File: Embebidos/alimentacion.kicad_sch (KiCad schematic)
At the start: 20 parts, among them J1 Conn_01x02_Male, J2 Conn_01x02_Male, J4 Conn_01x02_Male, U1 MIC29302WT, U2 SPX3819M5-L-3-3, U4 MIC5219-3.3YM5

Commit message: Alimentacion
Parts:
- C1: value 100u -> (none)
- C10, C5, C7: value 10u -> (none)
- C11: value 0.1u -> (none)
- C2: value 1u -> (none); footprint Capacitor_SMD:C_0603_1608Metric_Pad1.08x0.95mm_HandSolder -> (none)
- C3: value 330u -> (none)
- C4: value 100n -> (none)
- C6: value 1u -> (none)
- J1, J2, J4: value Conn_01x02_Male -> (none)
- R1: value 100k -> (none)
- R2: value 43k -> (none)
- R3: value 470 -> (none)
- R4, R5: value R -> (none)
- U1: value MIC29302WT -> (none); footprint Package_TO_SOT_THT:TO-220-5_P3.4x3.7mm_StaggerEven_Lead3.8mm_Vertical -> (none)
- U2: value SPX3819M5-L-3-3 -> (none); footprint Package_TO_SOT_SMD:SOT-23-5 -> (none)
- U4: value MIC5219-3.3YM5 -> (none); footprint Package_TO_SOT_SMD:SOT-23-5 -> (none)
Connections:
- net Esp32: no longer U2.3 (EN), U4.3 (EN)
- net +3.3V renamed 3.3
- new net CtrlOnOff: U2.3 (EN), U4.3 (EN)

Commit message: Alimentacion
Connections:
- net 3.3 renamed +3.3V
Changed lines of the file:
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@@
   (junction (at 153.035 142.24) (diameter 0) (color 0 0 0 0)
   )
+  (junction (at 45.72 81.28) (diameter 0) (color 0 0 0 0)
+  )
   (junction (at 195.58 81.28) (diameter 0) (color 0 0 0 0)
   )
@@
   )
   (junction (at 134.62 163.195) (diameter 0) (color 0 0 0 0)
-  )
-  (junction (at 45.72 80.01) (diameter 0) (color 0 0 0 0)
   )
   (junction (at 139.7 81.28) (diameter 0) (color 0 0 0 0)
@@
     (stroke (width 0) (type default) (color 0 0 0 0))
   )
-  (wire (pts (xy 35.56 69.85) (xy 38.1 69.85))
-    (stroke (width 0) (type default) (color 0 0 0 0))
-  )
   (wire (pts (xy 191.77 142.24) (xy 191.77 146.685))
     (stroke (width 0) (type default) (color 0 0 0 0))
@@
     (stroke (width 0) (type default) (color 0 0 0 0))
   )
-  (wire (pts (xy 151.13 87.63) (xy 152.4 87.63))
-    (stroke (width 0) (type default) (color 0 0 0 0))
-  )
   (wire (pts (xy 134.62 163.195) (xy 138.43 163.195))
     (stroke (width 0) (type default) (color 0 0 0 0))
@@
     (stroke (width 0) (type default) (color 0 0 0 0))
   )
-  (wire (pts (xy 45.72 76.2) (xy 45.72 80.01))
-    (stroke (width 0) (type default) (color 0 0 0 0))
-  )
   (wire (pts (xy 182.245 153.67) (xy 182.245 163.195))
     (stroke (width 0) (type default) (color 0 0 0 0))
@@
     (stroke (width 0) (type default) (color 0 0 0 0))
   )
-  (wire (pts (xy 33.02 80.01) (xy 45.72 80.01))
+  (wire (pts (xy 33.02 81.28) (xy 45.72 81.28))
     (stroke (width 0) (type default) (color 0 0 0 0))
   )
@@
     (stroke (width 0) (type default) (color 0 0 0 0))
   )
+  (wire (pts (xy 45.72 76.2) (xy 45.72 81.28))
+    (stroke (width 0) (type default) (color 0 0 0 0))
+  )
   (wire (pts (xy 67.31 66.04) (xy 67.31 67.31))
     (stroke (width 0) (type default) (color 0 0 0 0))
@@
     (stroke (width 0) (type default) (color 0 0 0 0))
   )
-  (wire (pts (xy 33.02 68.58) (xy 33.02 80.01))
+  (wire (pts (xy 33.02 68.58) (xy 33.02 81.28))
     (stroke (width 0) (type default) (color 0 0 0 0))
   )
@@
     (stroke (width 0) (type default) (color 0 0 0 0))
   )
+  (wire (pts (xy 45.72 85.09) (xy 45.72 81.28))
+    (stroke (width 0) (type default) (color 0 0 0 0))
+  )
   (wire (pts (xy 111.76 163.195) (xy 134.62 163.195))
     (stroke (width 0) (type default) (color 0 0 0 0))
@@
     (stroke (width 0) (type default) (color 0 0 0 0))
   )
-  (global_label "3.3" (shape output) (at 195.58 77.47 0) (fields_autoplaced)
-    (effects (font (size 1.27 1.27)) (justify left))
-    (property "Intersheet References" "${INTERSHEET_REFS}" (id 0) (at 201.0169 77.3906 0)
-      (effects (font (size 1.27 1.27)) (justify left) hide)
-    )
-  )
-  (global_label "CtrlOnOff" (shape input) (at 35.56 69.85 270) (fields_autoplaced)
+  (global_label "CtrlOnOff" (shape input) (at 38.1 69.85 270) (fields_autoplaced)
     (effects (font (size 1.27 1.27)) (justify right))
-    (property "Intersheet References" "${INTERSHEET_REFS}" (id 0) (at 35.4806 80.9717 90)
+    (property "Intersheet References" "${INTERSHEET_REFS}" (id 0) (at 38.0206 80.9717 90)
       (effects (font (size 1.27 1.27)) (justify right) hide)
     )
@@
     )
   )
-  (global_label "CtrlOnOff" (shape input) (at 152.4 87.63 270) (fields_autoplaced)
+  (global_label "CtrlOnOff" (shape input) (at 151.13 87.63 270) (fields_autoplaced)
     (effects (font (size 1.27 1.27)) (justify right))
-    (property "Intersheet References" "${INTERSHEET_REFS}" (id 0) (at 152.3206 98.7517 90)
+    (property "Intersheet References" "${INTERSHEET_REFS}" (id 0) (at 151.0506 98.7517 90)
       (effects (font (size 1.27 1.27)) (justify right) hide)
     )
@@
     (property "Intersheet References" "${INTERSHEET_REFS}" (id 0) (at 124.3806 158.6533 90)
       (effects (font (size 1.27 1.27)) (justify right) hide)
-    )
-  )
-  (global_label "3.3" (shape output) (at 77.47 64.77 90) (fields_autoplaced)
-    (effects (font (size 1.27 1.27)) (justify left))
-    (property "Intersheet References" "${INTERSHEET_REFS}" (id 0) (at 77.3906 59.3331 90)
-      (effects (font (size 1.27 1.27)) (justify left) hide)
     )
   )
@@
     (pin "1")
   )
+  (symbol (lib_id "power:+3.3V") (at 77.47 64.77 0) (unit 1)
+    (in_bom yes) (on_board yes)
+    (property "Reference" "#PWR06" (id 0) (at 77.47 68.58 0)
+      (effects (font (size 1.27 1.27)) hide)
+    )
+    (property "Value" "" (id 1) (at 77.851 60.3758 0))
+    (property "Footprint" "" (id 2) (at 77.47 64.77 0)
+      (effects (font (size 1.27 1.27)) hide)
+    )
+    (property "Datasheet" "" (id 3) (at 77.47 64.77 0)
+      (effects (font (size 1.27 1.27)) hide)
+    )
+    (pin "1")
+  )
   (symbol (lib_id "Device:R") (at 67.31 82.55 0) (unit 1)
     (in_bom yes) (on_board yes) (fields_autoplaced)
@@
     (pin "2")
   )
-  (symbol (lib_id "power:GND") (at 45.72 80.01 0) (unit 1)
-    (in_bom yes) (on_board yes) (fields_autoplaced)
-    (property "Reference" "#PWR03" (id 0) (at 45.72 86.36 0)
-      (effects (font (size 1.27 1.27)) hide)
-    )
-    (property "Value" "" (id 1) (at 45.72 85.09 0))
-    (property "Footprint" "" (id 2) (at 45.72 80.01 0)
-      (effects (font (size 1.27 1.27)) hide)
-    )
-    (property "Datasheet" "" (id 3) (at 45.72 80.01 0)
+  (symbol (lib_id "power:GND") (at 45.72 85.09 0) (unit 1)
+    (in_bom yes) (on_board yes) (fields_autoplaced)
+    (property "Reference" "#PWR03" (id 0) (at 45.72 91.44 0)
+      (effects (font (size 1.27 1.27)) hide)
+    )
+    (property "Value" "" (id 1) (at 45.72 90.17 0))
+    (property "Footprint" "" (id 2) (at 45.72 85.09 0)
+      (effects (font (size 1.27 1.27)) hide)
+    )
+    (property "Datasheet" "" (id 3) (at 45.72 85.09 0)
       (effects (font (size 1.27 1.27)) hide)
     )
@@
     (pin "2")
   )
+  (symbol (lib_id "power:+3.3V") (at 195.58 77.47 0) (unit 1)
+    (in_bom yes) (on_board yes)
+    (property "Reference" "#PWR011" (id 0) (at 195.58 81.28 0)
+      (effects (font (size 1.27 1.27)) hide)
+    )
+    (property "Value" "" (id 1) (at 195.961 73.0758 0))
+    (property "Footprint" "" (id 2) (at 195.58 77.47 0)
+      (effects (font (size 1.27 1.27)) hide)
+    )
+    (property "Datasheet" "" (id 3) (at 195.58 77.47 0)
+      (effects (font (size 1.27 1.27)) hide)
+    )
+    (pin "1")
+  )
   (symbol (lib_id "power:+5V") (at 91.44 140.97 0) (unit 1)

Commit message: Corrección de anotaciones
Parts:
- C10: renamed from C5; value (none) -> 10u
- C11: renamed from C6; value (none) -> 1u
- C12: renamed from C1; value (none) -> 100u
- C13: renamed from C2; value (none) -> 1u; footprint (none) -> Capacitor_SMD:C_0603_1608Metric_Pad1.08x0.95mm_HandSolder
- C14: renamed from C7; value (none) -> 10u
- C15: renamed from C3; value (none) -> 330u
- C16: renamed from C4; value (none) -> 100n
- C17: renamed from C10; value (none) -> 10u
- C18: renamed from C11; value (none) -> 0.1u
- J2: renamed from J1; value (none) -> Conn_01x02_Male
- J3: renamed from J2; value (none) -> Conn_01x02_Male
- J4: value (none) -> Conn_01x02_Male
- R18: renamed from R4; value (none) -> R
- R19: renamed from R5; value (none) -> R
- R20: renamed from R1; value (none) -> 100k
- R21: renamed from R2; value (none) -> 43k
- R22: renamed from R3; value (none) -> 470
- U3: renamed from U2; value (none) -> SPX3819M5-L-3-3; footprint (none) -> Package_TO_SOT_SMD:SOT-23-5
- U4: renamed from U1; value (none) -> MIC29302WT; footprint (none) -> Package_TO_SOT_THT:TO-220-5_P3.4x3.7mm_StaggerEven_Lead3.8mm_Vertical
- U5: renamed from U4; value (none) -> MIC5219-3.3YM5; footprint (none) -> Package_TO_SOT_SMD:SOT-23-5
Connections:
- no-connect marks 1 -> 0

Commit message: error_elc
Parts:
- removed J2, J4: Conn_01x02_Male, symbol Connector:Conn_01x02_Male
- renumbered C12 to C1, C17 to C10, C18 to C11, C13 to C2, C15 to C3, C16 to C4, C10 to C5, C11 to C6, C14 to C7, J3 to J2, R20 to R1, R21 to R2, R22 to R3, R18 to R4, R19 to R5, U4 to U1, U3 to U2, U5 to U4
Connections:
- net +3.3V: no longer C10.1, C11.1, U4.5 (OUT)
- net +5V: now also C7.1, U2.1 (IN), U4.1 (IN)
- new net 3.3Vop2: C10.1, C11.1, U4.5 (OUT)
- no-connect marks 0 -> 1

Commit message: anotaciones_fix
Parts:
- renumbered C5 to C10, C6 to C11, C1 to C12, C2 to C13, C7 to C14, C3 to C15, C4 to C16, C10 to C17, C11 to C18, R4 to R19, R5 to R20, R1 to R21, R2 to R22, R3 to R23, U2 to U3, U1 to U4, U4 to U5
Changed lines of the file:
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@@
   (symbol (lib_id "power:GND") (at 138.43 168.275 0) (unit 1)
     (in_bom yes) (on_board yes) (fields_autoplaced)
-    (property "Reference" "#PWR02" (id 0) (at 138.43 174.625 0)
+    (property "Reference" "#PWR031" (id 0) (at 138.43 174.625 0)
       (effects (font (size 1.27 1.27)) hide)
     )
@@
   (symbol (lib_id "Device:C") (at 139.7 87.63 0) (unit 1)
     (in_bom yes) (on_board yes) (fields_autoplaced)
-    (property "Reference" "C7" (id 0) (at 143.51 86.3599 0)
+    (property "Reference" "C14" (id 0) (at 143.51 86.3599 0)
       (effects (font (size 1.27 1.27)) (justify left))
     )
@@
   (symbol (lib_id "power:GND") (at 67.31 90.17 0) (unit 1)
     (in_bom yes) (on_board yes) (fields_autoplaced)
-    (property "Reference" "#PWR05" (id 0) (at 67.31 96.52 0)
+    (property "Reference" "#PWR026" (id 0) (at 67.31 96.52 0)
       (effects (font (size 1.27 1.27)) hide)
     )
@@
   (symbol (lib_id "Regulator_Linear:MIC29302WT") (at 134.62 144.78 0) (unit 1)
     (in_bom yes) (on_board yes)
-    (property "Reference" "U1" (id 0) (at 134.62 134.62 0))
+    (property "Reference" "U4" (id 0) (at 134.62 134.62 0))
     (property "Value" "MIC29302WT" (id 1) (at 134.62 137.16 0))
     (property "Footprint" "Package_TO_SOT_THT:TO-220-5_P3.4x3.7mm_StaggerEven_Lead3.8mm_Vertical" (id 2) (at 96.52 126.365 90)
@@
   (symbol (lib_id "power:GND") (at 139.7 96.52 0) (unit 1)
     (in_bom yes) (on_board yes) (fields_autoplaced)
-    (property "Reference" "#PWR08" (id 0) (at 139.7 102.87 0)
+    (property "Reference" "#PWR032" (id 0) (at 139.7 102.87 0)
       (effects (font (size 1.27 1.27)) hide)
     )
@@
   (symbol (lib_id "power:GND") (at 57.15 80.01 0) (unit 1)
     (in_bom yes) (on_board yes) (fields_autoplaced)
-    (property "Reference" "#PWR04" (id 0) (at 57.15 86.36 0)
+    (property "Reference" "#PWR025" (id 0) (at 57.15 86.36 0)
       (effects (font (size 1.27 1.27)) hide)
     )
@@
   (symbol (lib_id "Device:C") (at 182.245 149.86 0) (unit 1)
     (in_bom yes) (on_board yes)
-    (property "Reference" "C4" (id 0) (at 186.055 148.5899 0)
+    (property "Reference" "C16" (id 0) (at 186.055 148.5899 0)
       (effects (font (size 1.27 1.27)) (justify left))
     )
@@
   (symbol (lib_id "power:GND") (at 162.56 99.06 0) (unit 1)
     (in_bom yes) (on_board yes) (fields_autoplaced)
-    (property "Reference" "#PWR010" (id 0) (at 162.56 105.41 0)
+    (property "Reference" "#PWR033" (id 0) (at 162.56 105.41 0)
       (effects (font (size 1.27 1.27)) hide)
     )
@@
   (symbol (lib_id "Device:C") (at 195.58 93.98 0) (unit 1)
     (in_bom yes) (on_board yes) (fields_autoplaced)
-    (property "Reference" "C11" (id 0) (at 199.39 92.7099 0)
+    (property "Reference" "C18" (id 0) (at 199.39 92.7099 0)
       (effects (font (size 1.27 1.27)) (justify left))
     )
@@
   (symbol (lib_id "Device:C") (at 111.76 148.59 0) (unit 1)
     (in_bom yes) (on_board yes) (fields_autoplaced)
-    (property "Reference" "C2" (id 0) (at 115.57 147.3199 0)
+    (property "Reference" "C13" (id 0) (at 115.57 147.3199 0)
       (effects (font (size 1.27 1.27)) (justify left))
     )
@@
   (symbol (lib_id "Device:R") (at 153.035 148.59 0) (unit 1)
     (in_bom yes) (on_board yes) (fields_autoplaced)
-    (property "Reference" "R1" (id 0) (at 155.575 147.3199 0)
+    (property "Reference" "R21" (id 0) (at 155.575 147.3199 0)
       (effects (font (size 1.27 1.27)) (justify left))
     )
@@
   (symbol (lib_id "Device:R") (at 191.77 150.495 0) (unit 1)
     (in_bom yes) (on_board yes)
-    (property "Reference" "R3" (id 0) (at 194.31 149.2249 0)
+    (property "Reference" "R23" (id 0) (at 194.31 149.2249 0)
       (effects (font (size 1.27 1.27)) (justify left))
     )
@@
   (symbol (lib_id "Device:R") (at 67.31 71.12 0) (unit 1)
     (in_bom yes) (on_board yes) (fields_autoplaced)
-    (property "Reference" "R4" (id 0) (at 69.85 69.8499 0)
+    (property "Reference" "R19" (id 0) (at 69.85 69.8499 0)
       (effects (font (size 1.27 1.27)) (justify left))
     )
@@
   (symbol (lib_id "power:GND") (at 77.47 78.74 0) (unit 1)
     (in_bom yes) (on_board yes) (fields_autoplaced)
-    (property "Reference" "#PWR07" (id 0) (at 77.47 85.09 0)
+    (property "Reference" "#PWR028" (id 0) (at 77.47 85.09 0)
       (effects (font (size 1.27 1.27)) hide)
     )
@@
   (symbol (lib_id "power:+3.3V") (at 77.47 64.77 0) (unit 1)
     (in_bom yes) (on_board yes)
-    (property "Reference" "#PWR06" (id 0) (at 77.47 68.58 0)
+    (property "Reference" "#PWR027" (id 0) (at 77.47 68.58 0)
       (effects (font (size 1.27 1.27)) hide)
     )
@@
   (symbol (lib_id "Device:R") (at 67.31 82.55 0) (unit 1)
     (in_bom yes) (on_board yes) (fields_autoplaced)
-    (property "Reference" "R5" (id 0) (at 69.85 81.2799 0)
+    (property "Reference" "R20" (id 0) (at 69.85 81.2799 0)
       (effects (font (size 1.27 1.27)) (justify left))
     )
@@
   (symbol (lib_id "power:GND") (at 45.72 85.09 0) (unit 1)
     (in_bom yes) (on_board yes) (fields_autoplaced)
-    (property "Reference" "#PWR03" (id 0) (at 45.72 91.44 0)
+    (property "Reference" "#PWR024" (id 0) (at 45.72 91.44 0)
       (effects (font (size 1.27 1.27)) hide)
     )
@@
   (symbol (lib_id "Device:R") (at 153.035 158.115 0) (unit 1)
     (in_bom yes) (on_board yes) (fields_autoplaced)
-    (property "Reference" "R2" (id 0) (at 155.575 156.8449 0)
+    (property "Reference" "R22" (id 0) (at 155.575 156.8449 0)
       (effects (font (size 1.27 1.27)) (justify left))
     )
@@
   (symbol (lib_id "Device:C_Polarized_Small_US") (at 171.45 149.86 0) (unit 1)
     (in_bom yes) (on_board yes)
-    (property "Reference" "C3" (id 0) (at 174.625 148.1581 0)
+    (property "Reference" "C15" (id 0) (at 174.625 148.1581 0)
       (effects (font (size 1.27 1.27)) (justify left))
     )
@@
   (symbol (lib_id "Regulator_Linear:SPX3819M5-L-3-3") (at 45.72 68.58 0) (unit 1)
     (in_bom yes) (on_board yes) (fields_autoplaced)
-    (property "Reference" "U2" (id 0) (at 45.72 58.42 0))
+    (property "Reference" "U3" (id 0) (at 45.72 58.42 0))
     (property "Value" "SPX3819M5-L-3-3" (id 1) (at 45.72 60.96 0))
     (property "Footprint" "Package_TO_SOT_SMD:SOT-23-5" (id 2) (at 45.72 60.325 0)
@@
   (symbol (lib_id "power:+5V") (at 135.89 73.66 0) (unit 1)
     (in_bom yes) (on_board yes) (fields_autoplaced)
-    (property "Reference" "#PWR0101" (id 0) (at 135.89 77.47 0)
-      (effects (font (size 1.27 1.27)) hide)
-    )
-    (property "Value" "+5V" (id 1) (at 135.89 68.58 0))
+    (property "Reference" "#PWR030" (id 0) (at 135.89 77.47 0)
+      (effects (font (size 1.27 1.27)) hide)
+    )
+    (property "Value" "" (id 1) (at 135.89 68.58 0))
     (property "Footprint" "" (id 2) (at 135.89 73.66 0)
       (effects (font (size 1.27 1.27)) hide)
@@
   (symbol (lib_id "Device:C") (at 57.15 73.66 0) (unit 1)
     (in_bom yes) (on_board yes) (fields_autoplaced)
-    (property "Reference" "C5" (id 0) (at 60.96 72.3899 0)
+    (property "Reference" "C10" (id 0) (at 60.96 72.3899 0)
       (effects (font (size 1.27 1.27)) (justify left))
     )
@@
   (symbol (lib_id "Regulator_Linear:MIC5219-3.3YM5") (at 162.56 83.82 0) (unit 1)
     (in_bom yes) (on_board yes) (fields_autoplaced)
-    (property "Reference" "U4" (id 0) (at 162.56 73.66 0))
+    (property "Reference" "U5" (id 0) (at 162.56 73.66 0))
     (property "Value" "MIC5219-3.3YM5" (id 1) (at 162.56 76.2 0))
     (property "Footprint" "Package_TO_SOT_SMD:SOT-23-5" (id 2) (at 162.56 75.565 0)
@@
   (symbol (lib_id "Device:C_Polarized_Small_US") (at 100.33 148.59 0) (unit 1)
     (in_bom yes) (on_board yes)
-    (property "Reference" "C1" (id 0) (at 103.505 146.8881 0)
+    (property "Reference" "C12" (id 0) (at 103.505 146.8881 0)
       (effects (font (size 1.27 1.27)) (justify left))
     )
@@
   (symbol (lib_id "power:+5V") (at 33.02 63.5 0) (unit 1)
     (in_bom yes) (on_board yes) (fields_autoplaced)
-    (property "Reference" "#PWR0102" (id 0) (at 33.02 67.31 0)
-      (effects (font (size 1.27 1.27)) hide)
-    )
-    (property "Value" "+5V" (id 1) (at 33.02 58.42 0))
+    (property "Reference" "#PWR023" (id 0) (at 33.02 67.31 0)
+      (effects (font (size 1.27 1.27)) hide)
+    )
+    (property "Value" "" (id 1) (at 33.02 58.42 0))
     (property "Footprint" "" (id 2) (at 33.02 63.5 0)
       (effects (font (size 1.27 1.27)) hide)
@@
   (symbol (lib_id "Device:C") (at 182.88 93.98 0) (unit 1)
     (in_bom yes) (on_board yes) (fields_autoplaced)
-    (property "Reference" "C10" (id 0) (at 186.69 92.7099 0)
+    (property "Reference" "C17" (id 0) (at 186.69 92.7099 0)
       (effects (font (size 1.27 1.27)) (justify left))
     )
@@
   (symbol (lib_id "Device:C_Polarized") (at 77.47 72.39 0) (unit 1)
     (in_bom yes) (on_board yes) (fields_autoplaced)
-    (property "Reference" "C6" (id 0) (at 81.28 70.2309 0)
+    (property "Reference" "C11" (id 0) (at 81.28 70.2309 0)
       (effects (font (size 1.27 1.27)) (justify left))
     )
@@
   (symbol (lib_id "power:+5V") (at 91.44 140.97 0) (unit 1)
     (in_bom yes) (on_board yes) (fields_autoplaced)
-    (property "Reference" "#PWR01" (id 0) (at 91.44 144.78 0)
-      (effects (font (size 1.27 1.27)) hide)
-    )
+    (property "Reference" "#PWR029" (id 0) (at 91.44 144.78 0)
+      (effects (font (size 1.27 1.27)) hide)
+    )

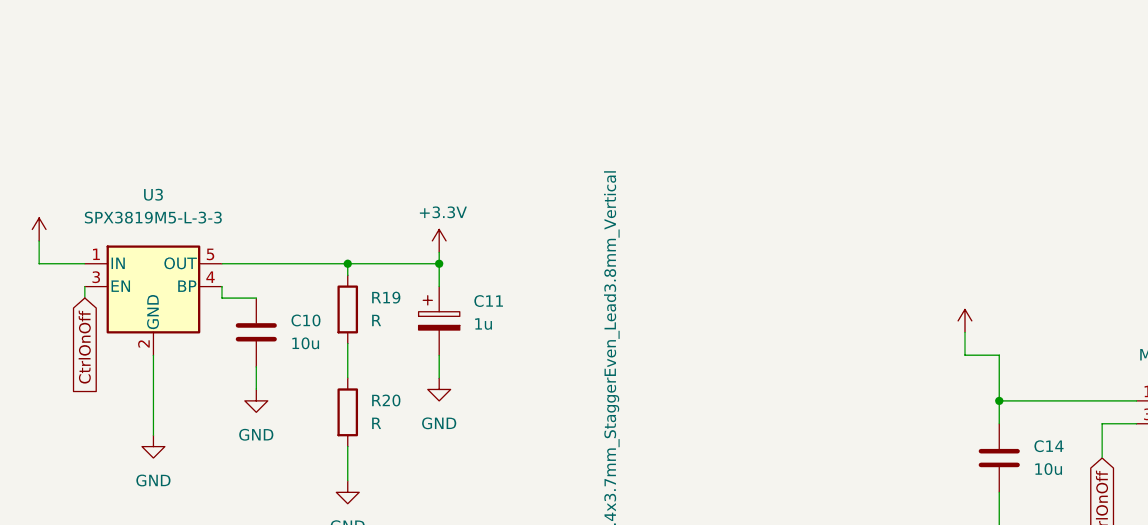
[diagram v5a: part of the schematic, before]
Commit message: conectoresRFySIM
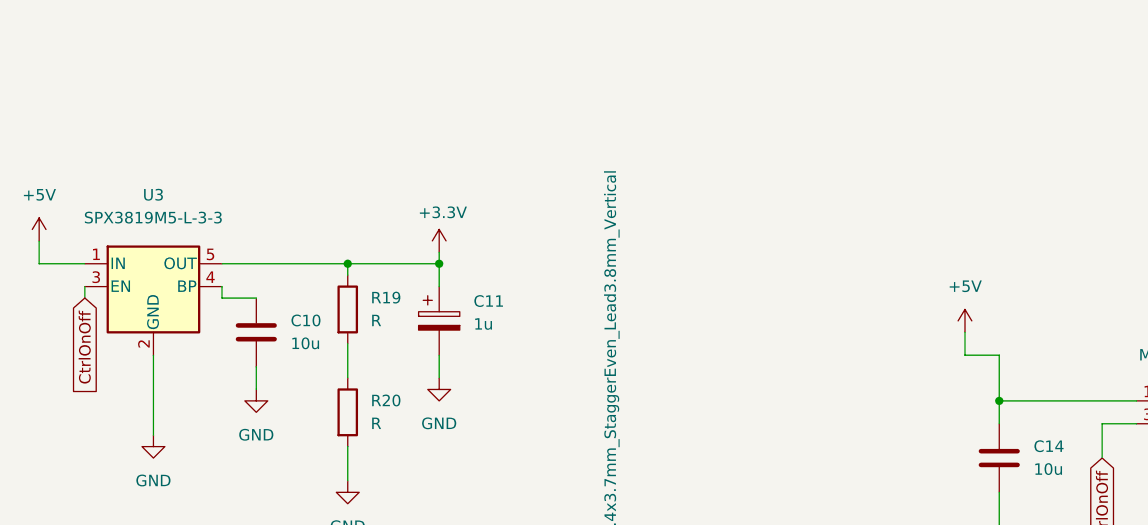
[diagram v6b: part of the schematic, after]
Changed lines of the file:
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@@
       (effects (font (size 1.27 1.27)) hide)
     )
-    (property "Value" "" (id 1) (at 135.89 68.58 0))
+    (property "Value" "+5V" (id 1) (at 135.89 68.58 0))
     (property "Footprint" "" (id 2) (at 135.89 73.66 0)
       (effects (font (size 1.27 1.27)) hide)
@@
       (effects (font (size 1.27 1.27)) hide)
     )
-    (property "Value" "" (id 1) (at 33.02 58.42 0))
+    (property "Value" "+5V" (id 1) (at 33.02 58.42 0))
     (property "Footprint" "" (id 2) (at 33.02 63.5 0)
       (effects (font (size 1.27 1.27)) hide)

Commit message: mejoras alimentacion
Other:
- note added: "Alimentacion con regulador a 4.1V usado para alimentar unicamente el modulo SIM"
- note added: "Alimentacion con regulador de 3.3V para la ESP32. las R sobran se pueden usar para regular"
- note added: "Alimentacion de 3.3V GPS LDR RFID se deja un regulador separado para poder controlar el funcionamiento de algunos modulos sin desactivar la alimentacion de la ESP32"
- moved on the sheet: C12, C13, C15, C16, J2, R21, R22, R23, U4

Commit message: se agrego el bonito
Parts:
- added JP1: Jumper_2_Bridged, symbol Jumper:Jumper_2_Bridged
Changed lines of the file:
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@@
+    (pin "2")
+  )
+  (symbol (lib_id "Jumper:Jumper_2_Bridged") (at 182.88 29.21 0) (unit 1)
+    (in_bom yes) (on_board yes) (fields_autoplaced)
+    (property "Reference" "JP1" (id 0) (at 182.88 22.86 0))
+    (property "Value" "Jumper_2_Bridged" (id 1) (at 182.88 25.4 0))
+    (property "Footprint" "" (id 2) (at 182.88 29.21 0)
+      (effects (font (size 1.27 1.27)) hide)
+    )
+    (property "Datasheet" "~" (id 3) (at 182.88 29.21 0)
+      (effects (font (size 1.27 1.27)) hide)
+    )
+    (pin "1")
     (pin "2")
   )
